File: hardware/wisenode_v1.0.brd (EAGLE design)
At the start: 50 x 50 mm, 33 parts, among them J1 AUDIO-JACK2PTH, J2 M04X2, Q1 G2XX3---PW20, Q4 32.768 kHz, U1 MIC5025-3.3, X1 USBSMD

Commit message: schematic .png
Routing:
- net GND: track 208.0 -> 209.4 mm
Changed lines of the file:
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@@
 <wire x1="1.905" y1="15.24" x2="4.699" y2="15.24" width="0.3048" layer="16"/>
 <wire x1="4.699" y1="15.24" x2="5.08" y2="15.24" width="0.3048" layer="16"/>
+<wire x1="18.542" y1="6.223" x2="18.1" y2="6.223" width="0.3048" layer="1"/>
+<wire x1="18.1" y1="6.223" x2="17.018" y2="7.305" width="0.3048" layer="1"/>
 <wire x1="48.641" y1="6.096" x2="49.022" y2="2.159" width="0" layer="19" extent="1-1"/>
 <wire x1="34.036" y1="12.7" x2="33.567" y2="15.748" width="0" layer="19" extent="1-1"/>
-<wire x1="10.287" y1="8.636" x2="11.557" y2="9.017" width="0" layer="19" extent="16-16"/>
 <wire x1="22.098" y1="1.143" x2="24.677" y2="3.683" width="0" layer="19" extent="1-1"/>
-<wire x1="18.542" y1="6.223" x2="18.1" y2="6.223" width="0.3048" layer="1"/>
-<wire x1="18.1" y1="6.223" x2="17.018" y2="7.305" width="0.3048" layer="1"/>
+<wire x1="11.557" y1="9.017" x2="10.668" y2="9.017" width="0.4064" layer="16"/>
+<wire x1="10.668" y1="9.017" x2="10.287" y2="8.636" width="0.4064" layer="16"/>
 </signal>
 <signal name="N$1">
@@
 <wire x1="16.703" y1="9.52" x2="17.018" y2="9.205" width="0.4064" layer="1"/>
 </signal>
-<signal name="N$12">
-</signal>
 <signal name="N$11">

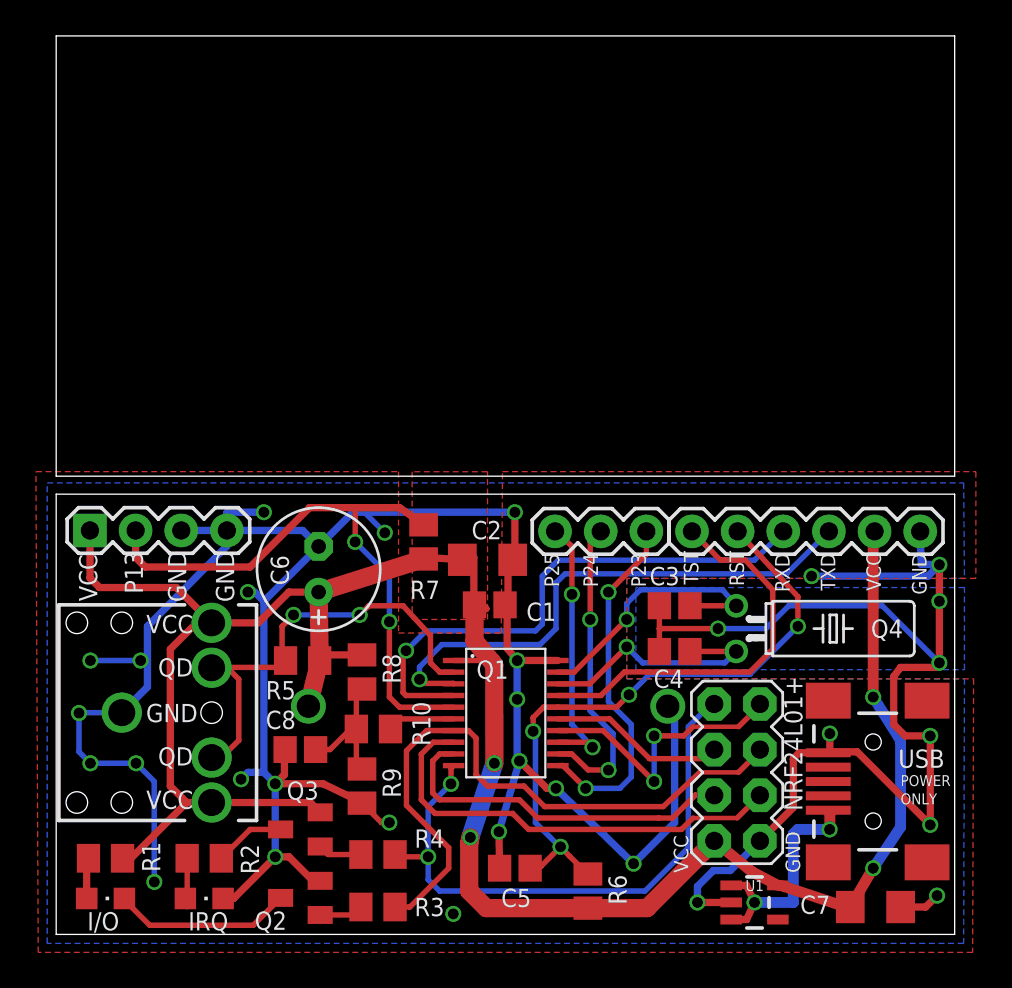
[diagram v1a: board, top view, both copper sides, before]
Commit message: fixed overlap of P2.5 header and coin cell holder
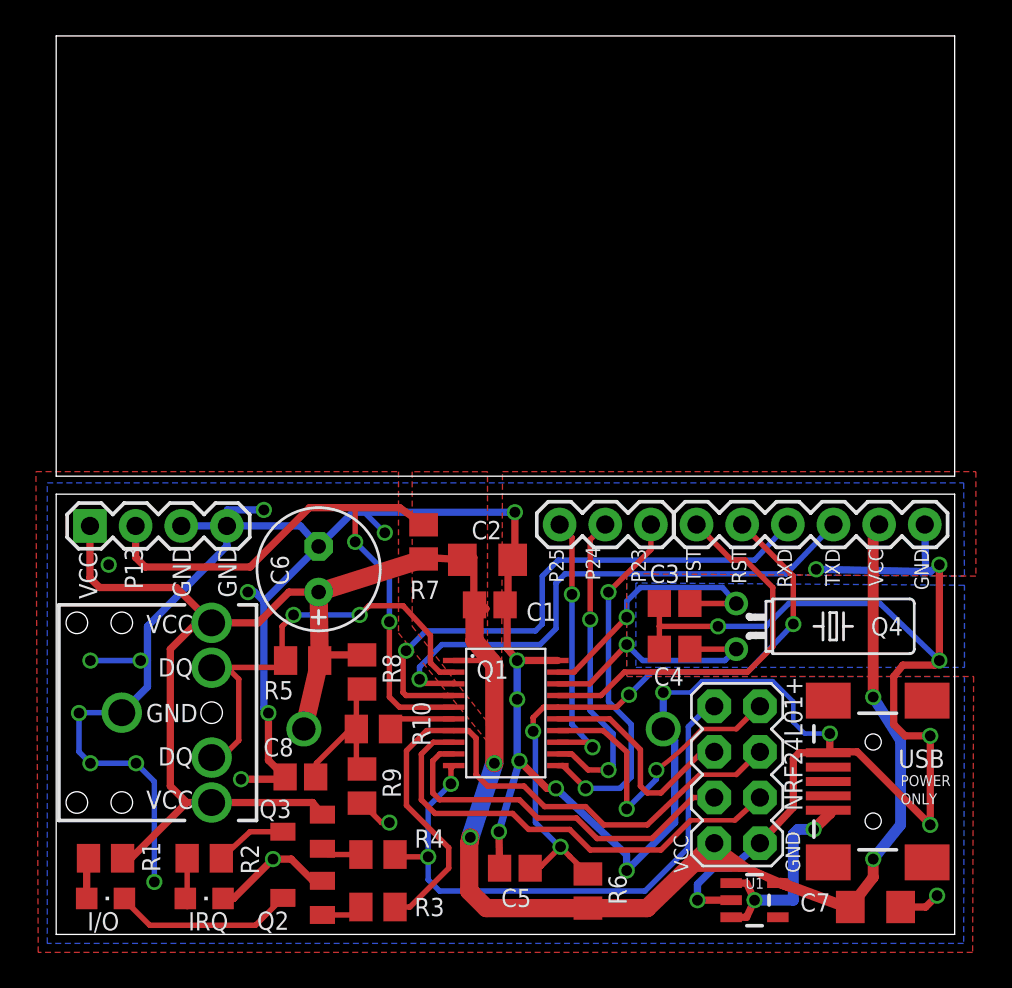
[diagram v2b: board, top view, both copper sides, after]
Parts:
- moved U$1 2.67 mm to (45.4, 6.31)
- moved C8 1.52 mm to (13.6, 8.76)
- moved BAT1 1.30 mm to (33.8, 11.4)
- moved J4 0.46 mm to (35.6, 22.8)
- moved JP1 0.46 mm to (28.0, 22.8)
- moved J3 0.25 mm to (1.88, 22.7)
- moved Q3 0.18 mm to (13.7, 5.71)
- moved C4 0.13 mm to (34.4, 15.9)
- moved U1 0.13 mm to (38.9, 1.91)
- moved C3 0.13 mm to (34.4, 18.4)
- moved J2 0.13 mm to (37.9, 8.89)
- moved Q2 0.13 mm to (13.7, 2.03)
- moved Q4 0.13 mm to (37.8, 17.1)
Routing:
- net +3V3: track 128.8 -> 143.6 mm
- net MOSI: track 9.82 -> 12.5 mm
- net GND: track 209.4 -> 211.6 mm
- net MISO: track 15.7 -> 17.5 mm
- net VBATT1: track 7.49 -> 8.53 mm
- net CSN: track 19.9 -> 20.8 mm
- net CE: track 24.9 -> 25.8 mm
- net SCLK: track 36.2 -> 37.0 mm
- net N$11: track 13.0 -> 12.4 mm
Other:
- board text added: "DQ"
- board text removed: "QD"

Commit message: BAT54A diode avoid charging battery
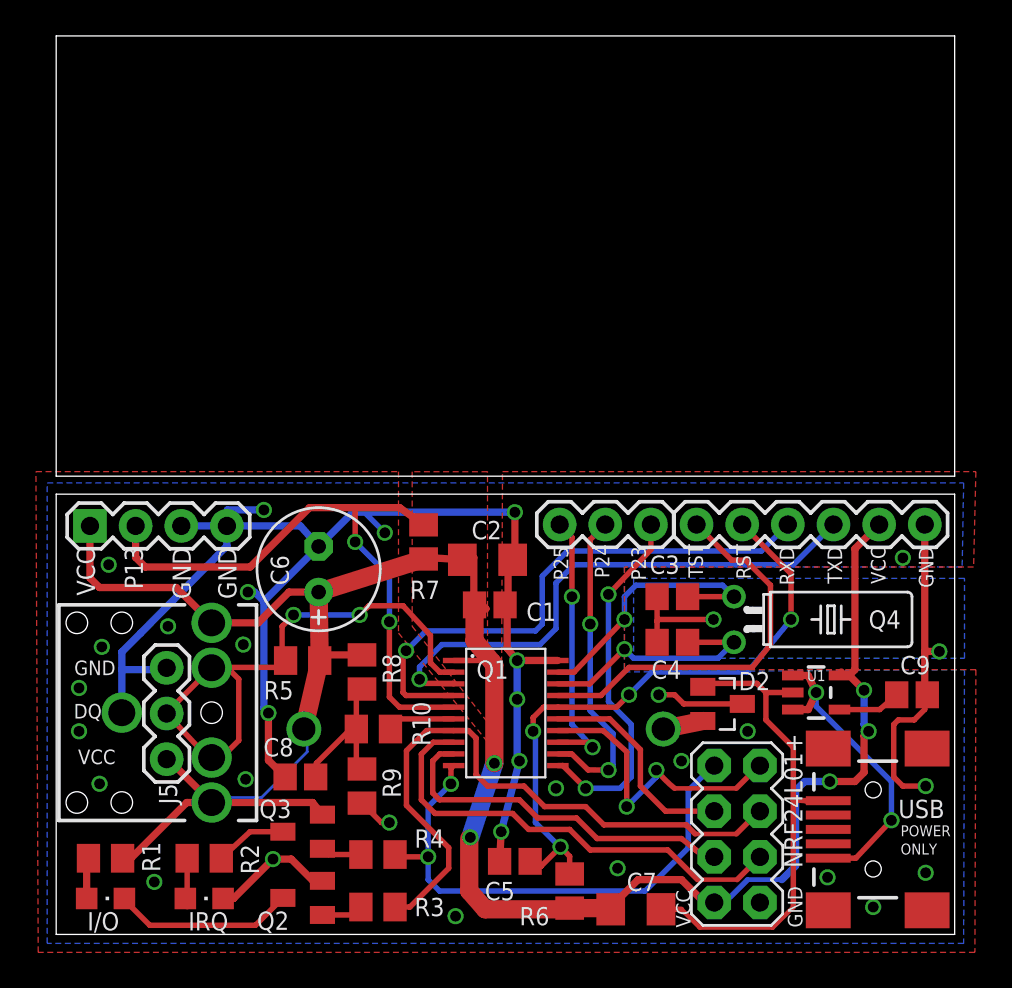
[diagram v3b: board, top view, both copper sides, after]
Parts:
- added C9: 470pF, resistor:C0805
- added D2: BAT54A, diode:SOT23
- added J5: (no value), SparkFun:1X03
- moved C7 13.3 mm to (32.3, 1.40)
- moved U1 12.1 mm to (42.3, 13.5)
- moved J2 3.30 mm to (37.9, 5.58)
- moved X1 2.67 mm to (45.5, 5.84)
- moved U$1 2.67 mm to (45.4, 3.64)
- moved R6 1.02 mm to (28.6, 2.41)
- moved C3 0.40 mm to (34.3, 18.8)
- moved C4 0.40 mm to (34.3, 16.3)
- moved Q4 0.40 mm to (37.7, 17.5)
- moved C5 0.38 mm to (25.5, 4.06)
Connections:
- new net N$11: C7.2, D2.1, U1.2, X1.GND
- new net N$13: BAT1.2, D2.2
- new net N$15: C9.2, U1.4
- net +3V3: now also J5.1
- net DQ: now also J5.2
- net GND: now also C9.1, D2.3, J5.3; no longer BAT1.2, C7.2, U1.2, X1.GND
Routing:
- net GND: track 211.6 -> 118.3 mm, vias 31 -> 33
- net N$11: track 0.00 -> 28.0 mm
- net +3V3: track 143.6 -> 128.5 mm, vias 4 -> 5
- net DQ: track 27.0 -> 33.6 mm
- net N$12: track 12.4 -> 17.1 mm
- net N$15: track 0.00 -> 3.49 mm
- net IRQ: track 33.2 -> 29.8 mm
- net N$13: track 0.00 -> 2.25 mm
- net SCLK: track 37.0 -> 36.1 mm
- net MISO: track 17.5 -> 16.8 mm
- net N$5: track 35.5 -> 34.9 mm
- net MOSI: track 12.5 -> 12.0 mm

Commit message: moved C7
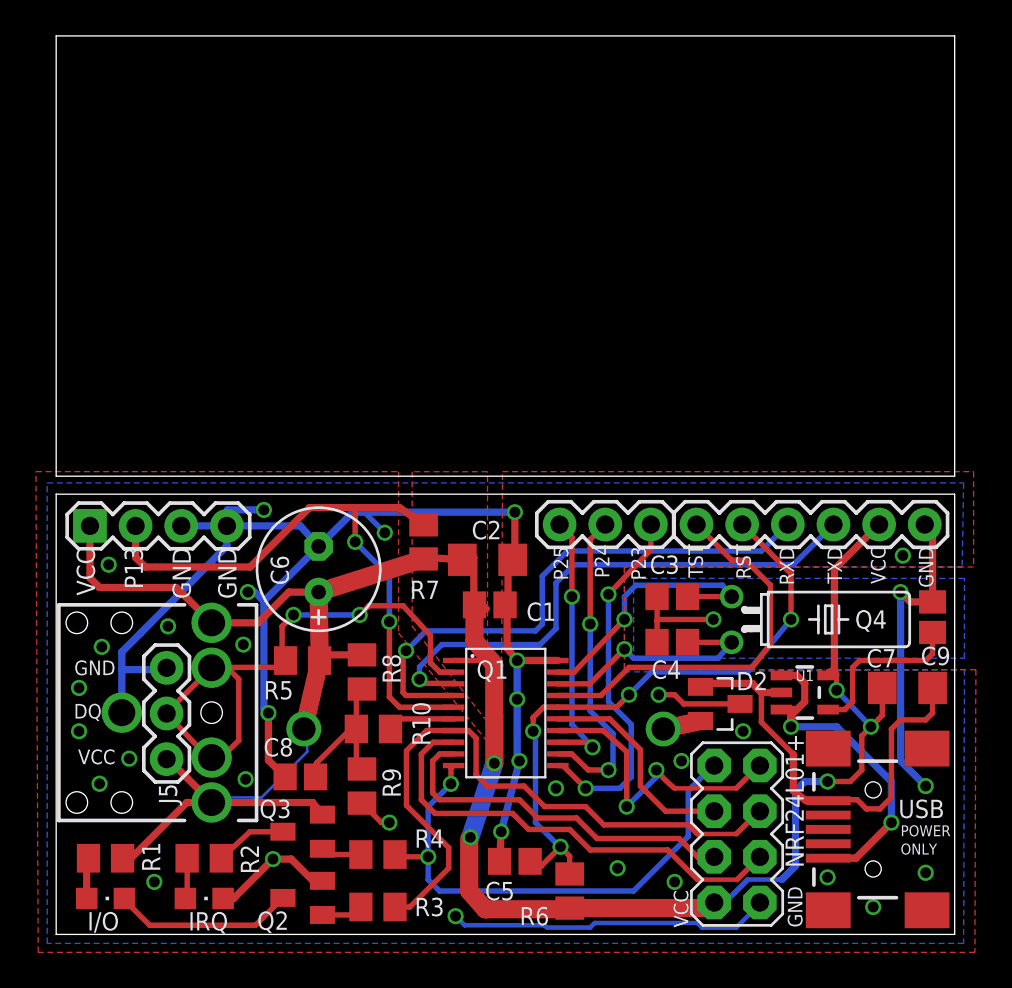
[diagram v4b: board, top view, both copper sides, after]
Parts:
- moved C7 19.5 mm to (47.4, 13.7)
- moved C9 4.47 mm to (48.8, 17.7), turned to 270 degrees
- moved U1 0.63 mm to (41.7, 13.5)
- moved D2 0.13 mm to (37.0, 12.8)
- moved Q4 0.13 mm to (37.6, 17.5)
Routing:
- net GND: track 118.3 -> 136.1 mm, vias 33 -> 35
- net N$15: track 3.49 -> 9.40 mm
- net N$11: track 28.0 -> 25.0 mm
- net N$12: track 17.1 -> 19.5 mm
- net +3V3: track 128.5 -> 130.4 mm
